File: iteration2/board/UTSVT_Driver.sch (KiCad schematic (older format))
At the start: 5 parts, among them J1 DB37_Female_MountingHoles, U1 Nucleo, U2 SN65HVD230, U3 CAN_adapter

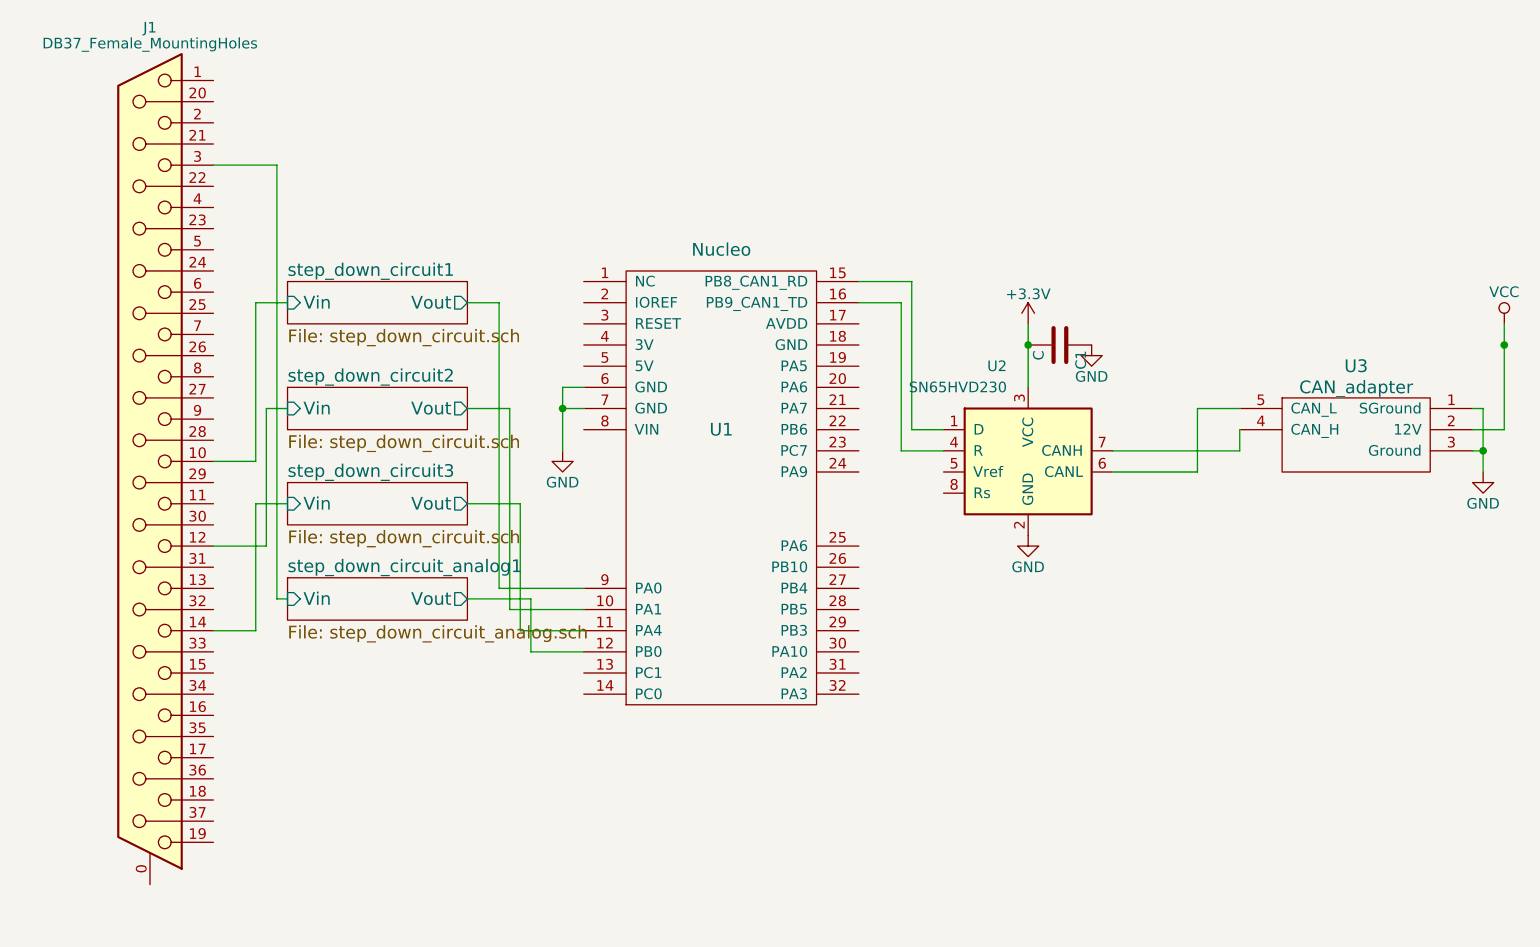
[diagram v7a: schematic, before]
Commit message: partially resolved merge issues and added script for automatic merging
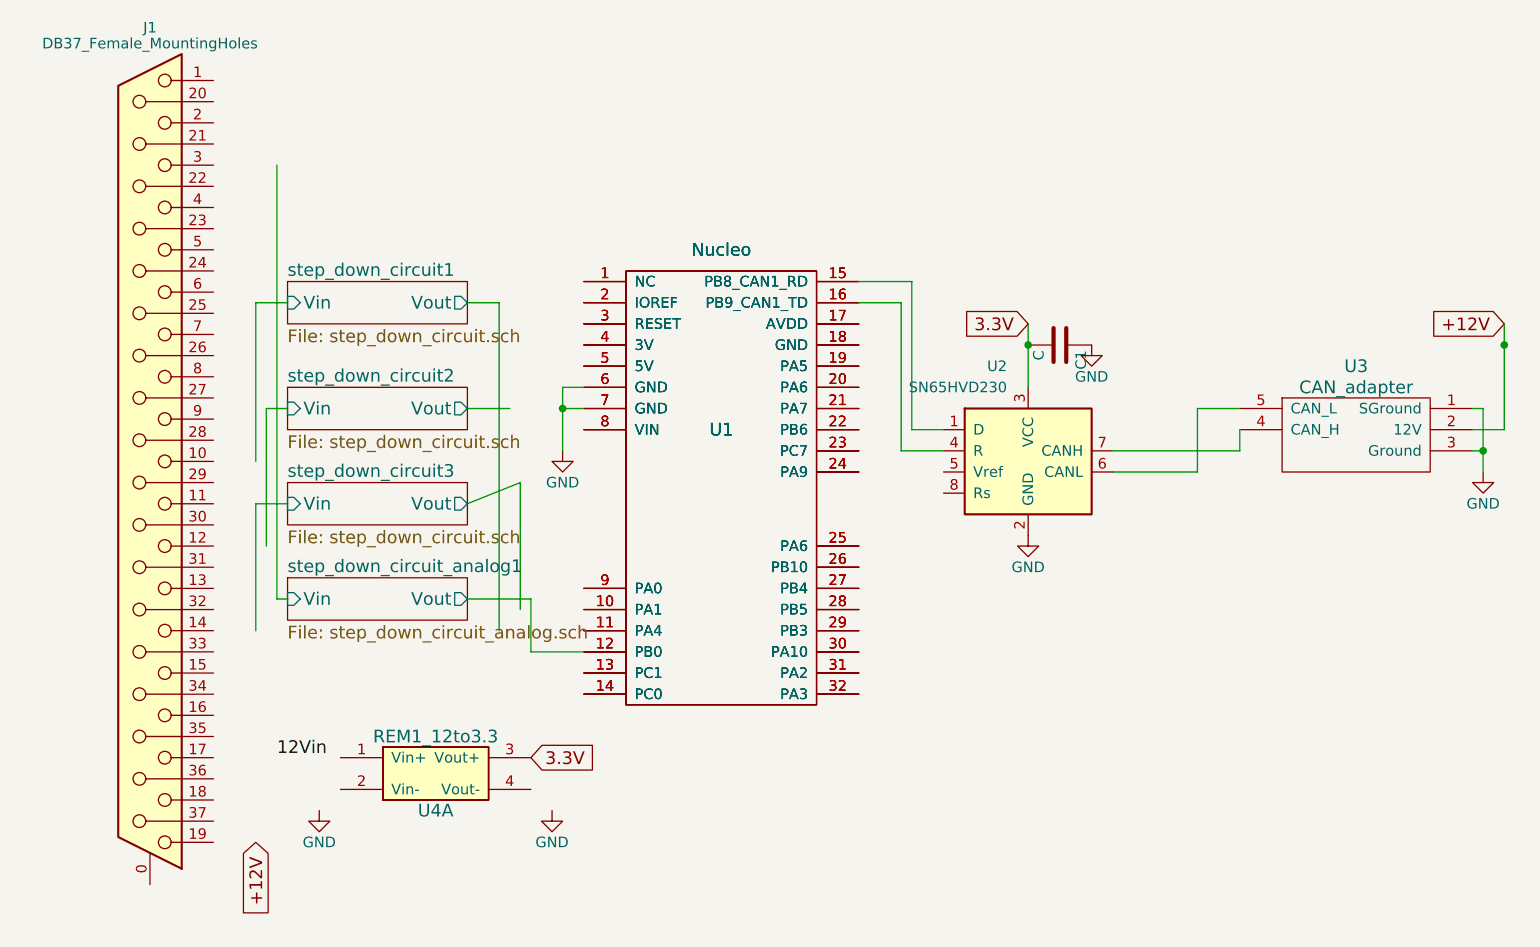
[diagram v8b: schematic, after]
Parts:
- added U4: REM1_12to3.3, MotorControllerStuff:REM1_12to3.3, symbol REM1_12to3.3
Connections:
- net labels added: +12V, 12Vin, 3.3V
- net labels removed: +3.3V, VCC
- wire segments 44 -> 36
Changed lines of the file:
@@
 $EndComp
 $Comp
-L GND #PWR01
+L GND #PWR6
 U 1 1 59F244D9
 P 9700 3950
-F 0 "#PWR01" H 9700 3700 50  0001 C CNN
+F 0 "#PWR6" H 9700 3700 50  0001 C CNN
 F 1 "GND" H 9700 3800 50  0000 C CNN
 F 2 "" H 9700 3950 50  0001 C CNN
@@
 $EndComp
 $Comp
-L GND #PWR02
+L GND #PWR4
 U 1 1 59F24541
 P 7550 4250
-F 0 "#PWR02" H 7550 4000 50  0001 C CNN
+F 0 "#PWR4" H 7550 4000 50  0001 C CNN
 F 1 "GND" H 7550 4100 50  0000 C CNN
 F 2 "" H 7550 4250 50  0001 C CNN
@@
 $EndComp
 $Comp
-L GND #PWR03
+L GND #PWR3
 U 1 1 59F262C8
 P 5350 3850
-F 0 "#PWR03" H 5350 3600 50  0001 C CNN
+F 0 "#PWR3" H 5350 3600 50  0001 C CNN
 F 1 "GND" H 5350 3700 50  0000 C CNN
 F 2 "" H 5350 3850 50  0001 C CNN
 F 3 "" H 5350 3850 50  0001 C CNN
 	1    5350 3850
-	1    0    0    -1
-$EndComp
-$Comp
-L VCC #PWR04
-U 1 1 59F2677A
-P 9800 3250
-F 0 "#PWR04" H 9800 3100 50  0001 C CNN
-F 1 "VCC" H 9800 3400 50  0000 C CNN
-F 2 "" H 9800 3250 50  0001 C CNN
-F 3 "" H 9800 3250 50  0001 C CNN
-	1    9800 3250
 	1    0    0    -1
 $EndComp
@@
 $EndSheet
 $Comp
-L GND #PWR05
+L GND #PWR5
 U 1 1 59F29663
 P 7850 3350
-F 0 "#PWR05" H 7850 3100 50  0001 C CNN
+F 0 "#PWR5" H 7850 3100 50  0001 C CNN
 F 1 "GND" H 7850 3200 50  0000 C CNN
 F 2 "" H 7850 3350 50  0001 C CNN
 F 3 "" H 7850 3350 50  0001 C CNN
 	1    7850 3350
-	1    0    0    -1
-$EndComp
-$Comp
-L +3.3V #PWR06
-U 1 1 59F296AF
-P 7550 3250
-F 0 "#PWR06" H 7550 3100 50  0001 C CNN
-F 1 "+3.3V" H 7550 3390 50  0000 C CNN
-F 2 "" H 7550 3250 50  0001 C CNN
-F 3 "" H 7550 3250 50  0001 C CNN
-	1    7550 3250
 	1    0    0    -1
 $EndComp
@@
 	0    1    1    0
 $EndComp
+$Comp
+L Nucleo U1
+U 1 1 59F29930
+P 6100 4050
+F 0 "U1" H 6100 4350 60  0000 C CNN
+F 1 "Nucleo" H 6100 5200 60  0000 C CNN
+F 2 "UTSVT_board:AFBShieldBoard" H 6100 4350 60  0001 C CNN
+F 3 "" H 6100 4350 60  0001 C CNN
+	1    6100 4050
+	1    0    0    -1
+$EndComp
+$Comp
+L REM1_12to3.3 U4
+U 1 1 59F4D82D
+P 4750 5400
+F 0 "U4" H 4750 5250 60  0000 C CNN
+F 1 "REM1_12to3.3" H 4750 5600 60  0000 C CNN
+F 2 "MotorControllerStuff:REM1_12to3.3" H 4750 5600 60  0001 C CNN
+F 3 "" H 4750 5600 60  0001 C CNN
+	1    4750 5400
+	1    0    0    -1
+$EndComp
+Text Label 4000 5300 0    60   ~ 0
+12Vin
+$Comp
+L GND #PWR1
+U 1 1 59F4EAEA
+P 4200 5550
+F 0 "#PWR1" H 4200 5300 50  0001 C CNN
+F 1 "GND" H 4200 5400 50  0000 C CNN
+F 2 "" H 4200 5550 50  0001 C CNN
+F 3 "" H 4200 5550 50  0001 C CNN
+	1    4200 5550
+	1    0    0    -1
+$EndComp
+Text GLabel 5200 5300 2    60   Input ~ 0
+3.3V
+$Comp
+L GND #PWR2
+U 1 1 59F4F385
+P 5300 5550
+F 0 "#PWR2" H 5300 5300 50  0001 C CNN
+F 1 "GND" H 5300 5400 50  0000 C CNN
+F 2 "" H 5300 5550 50  0001 C CNN
+F 3 "" H 5300 5550 50  0001 C CNN
+	1    5300 5550
+	1    0    0    -1
+$EndComp
+Text GLabel 7550 3250 0    60   Input ~ 0
+3.3V
+Text GLabel 3900 5700 3    60   Input ~ 0
++12V
+Text GLabel 9800 3250 0    60   Input ~ 0
++12V
 Wire Wire Line
 	7950 3850 8550 3850
@@
 	4900 3150 5050 3150
 Wire Wire Line
-	5050 3150 5050 4500
-Wire Wire Line
-	5050 4500 5450 4500
+	5050 3150 5050 4700
 Wire Wire Line
 	4900 3650 5100 3650
 Wire Wire Line
-	5100 3650 5100 4600
+	4900 4100 5150 4000
 Wire Wire Line
-	5100 4600 5450 4600
-Wire Wire Line
-	4900 4100 5150 4100
-Wire Wire Line
-	5150 4100 5150 4700
-Wire Wire Line
-	5150 4700 5450 4700
-Wire Wire Line
-	3700 2500 4000 2500
+	5150 4000 5150 4600
 Wire Wire Line
 	4000 2500 4000 4550
@@
 	4000 4550 4050 4550
 Wire Wire Line
-	3700 4300 3950 4300
-Wire Wire Line
 	3950 4300 3950 3650
 Wire Wire Line
 	3950 3650 4050 3650
-Wire Wire Line
-	3700 3900 3900 3900
 Wire Wire Line
 	3900 3900 3900 3150
@@
 	3900 3150 4050 3150
 Wire Wire Line
-	3700 4700 3900 4700
-Wire Wire Line
 	3900 4700 3900 4100
